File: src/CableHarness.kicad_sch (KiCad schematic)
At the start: 14 parts, among them J93 Car Socket

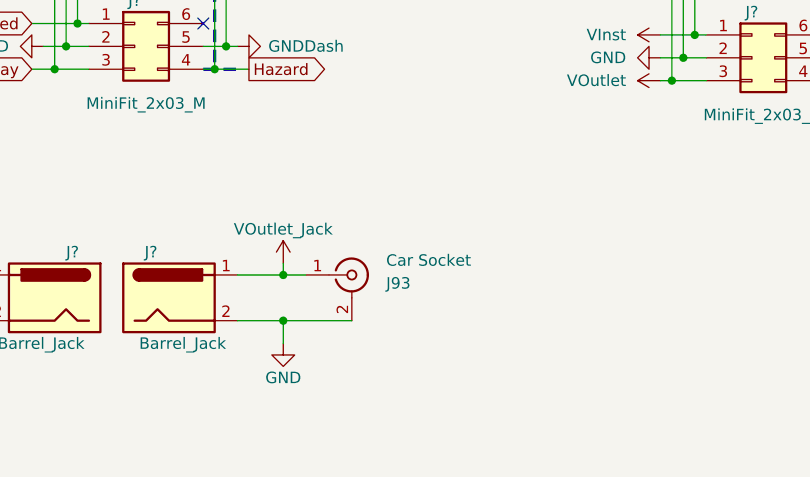
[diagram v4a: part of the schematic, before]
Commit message: Update Schematics; Replace xor with quad nand; Update PCB
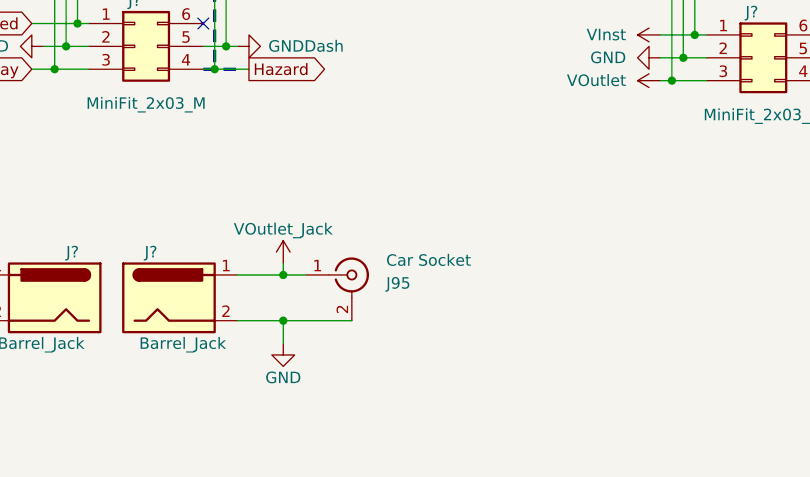
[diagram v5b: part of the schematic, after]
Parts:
- renumbered J93 to J95
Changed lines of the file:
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@@
   (symbol (lib_id "Connector:Conn_Coaxial") (at 195.58 148.59 0) (unit 1)
     (in_bom yes) (on_board yes) (dnp no) (fields_autoplaced)
-    (property "Reference" "J93" (at 199.39 149.5182 0)
+    (property "Reference" "J95" (at 199.39 149.5182 0)
       (effects (font (size 1.27 1.27)) (justify left))
     )
@@
       (project "dragstar-infotainment"
         (path "/e63e39d7-6ac0-4ffd-8aa3-1841a4541b55/74c2db39-21c2-4028-99b6-acc90560d53b"
-          (reference "J93") (unit 1)
+          (reference "J95") (unit 1)
         )
       )
@@
         )
         (path "/e63e39d7-6ac0-4ffd-8aa3-1841a4541b55/74c2db39-21c2-4028-99b6-acc90560d53b"
-          (reference "J87") (unit 1)
+          (reference "J89") (unit 1)
         )
       )
@@
         )
         (path "/e63e39d7-6ac0-4ffd-8aa3-1841a4541b55/74c2db39-21c2-4028-99b6-acc90560d53b"
-          (reference "J88") (unit 1)
+          (reference "J90") (unit 1)
         )
       )
@@
         )
         (path "/e63e39d7-6ac0-4ffd-8aa3-1841a4541b55/74c2db39-21c2-4028-99b6-acc90560d53b"
-          (reference "J86") (unit 1)
+          (reference "J88") (unit 1)
         )
       )
@@
         )
         (path "/e63e39d7-6ac0-4ffd-8aa3-1841a4541b55/74c2db39-21c2-4028-99b6-acc90560d53b"
-          (reference "J92") (unit 1)
+          (reference "J94") (unit 1)
         )
         (path "/e63e39d7-6ac0-4ffd-8aa3-1841a4541b55/5d40715c-dfc9-4b95-9cc7-adbd4b609d9b"
@@
         )
         (path "/e63e39d7-6ac0-4ffd-8aa3-1841a4541b55/74c2db39-21c2-4028-99b6-acc90560d53b"
-          (reference "J85") (unit 1)
+          (reference "J87") (unit 1)
         )
       )
@@
         )
         (path "/e63e39d7-6ac0-4ffd-8aa3-1841a4541b55/74c2db39-21c2-4028-99b6-acc90560d53b"
-          (reference "J84") (unit 1)
+          (reference "J86") (unit 1)
         )
       )
@@
         )
         (path "/e63e39d7-6ac0-4ffd-8aa3-1841a4541b55/74c2db39-21c2-4028-99b6-acc90560d53b"
-          (reference "J91") (unit 1)
+          (reference "J93") (unit 1)
         )
       )
@@
         )
         (path "/e63e39d7-6ac0-4ffd-8aa3-1841a4541b55/74c2db39-21c2-4028-99b6-acc90560d53b"
-          (reference "J90") (unit 1)
+          (reference "J92") (unit 1)
         )
       )
@@
         )
         (path "/e63e39d7-6ac0-4ffd-8aa3-1841a4541b55/74c2db39-21c2-4028-99b6-acc90560d53b"
-          (reference "J83") (unit 1)
+          (reference "J85") (unit 1)
         )
       )
@@
         )
         (path "/e63e39d7-6ac0-4ffd-8aa3-1841a4541b55/74c2db39-21c2-4028-99b6-acc90560d53b"
-          (reference "J82") (unit 1)
+          (reference "J84") (unit 1)
         )
       )
@@
         )
         (path "/e63e39d7-6ac0-4ffd-8aa3-1841a4541b55/74c2db39-21c2-4028-99b6-acc90560d53b"
-          (reference "J94") (unit 1)
+          (reference "J96") (unit 1)
         )
       )
@@
         )
         (path "/e63e39d7-6ac0-4ffd-8aa3-1841a4541b55/74c2db39-21c2-4028-99b6-acc90560d53b"
-          (reference "J89") (unit 1)
+          (reference "J91") (unit 1)
         )
         (path "/e63e39d7-6ac0-4ffd-8aa3-1841a4541b55/5d40715c-dfc9-4b95-9cc7-adbd4b609d9b"
@@
         )
         (path "/e63e39d7-6ac0-4ffd-8aa3-1841a4541b55/74c2db39-21c2-4028-99b6-acc90560d53b"
-          (reference "J95") (unit 1)
-        )
-      )
+          (reference "J97") (unit 1)
+        )
+      )

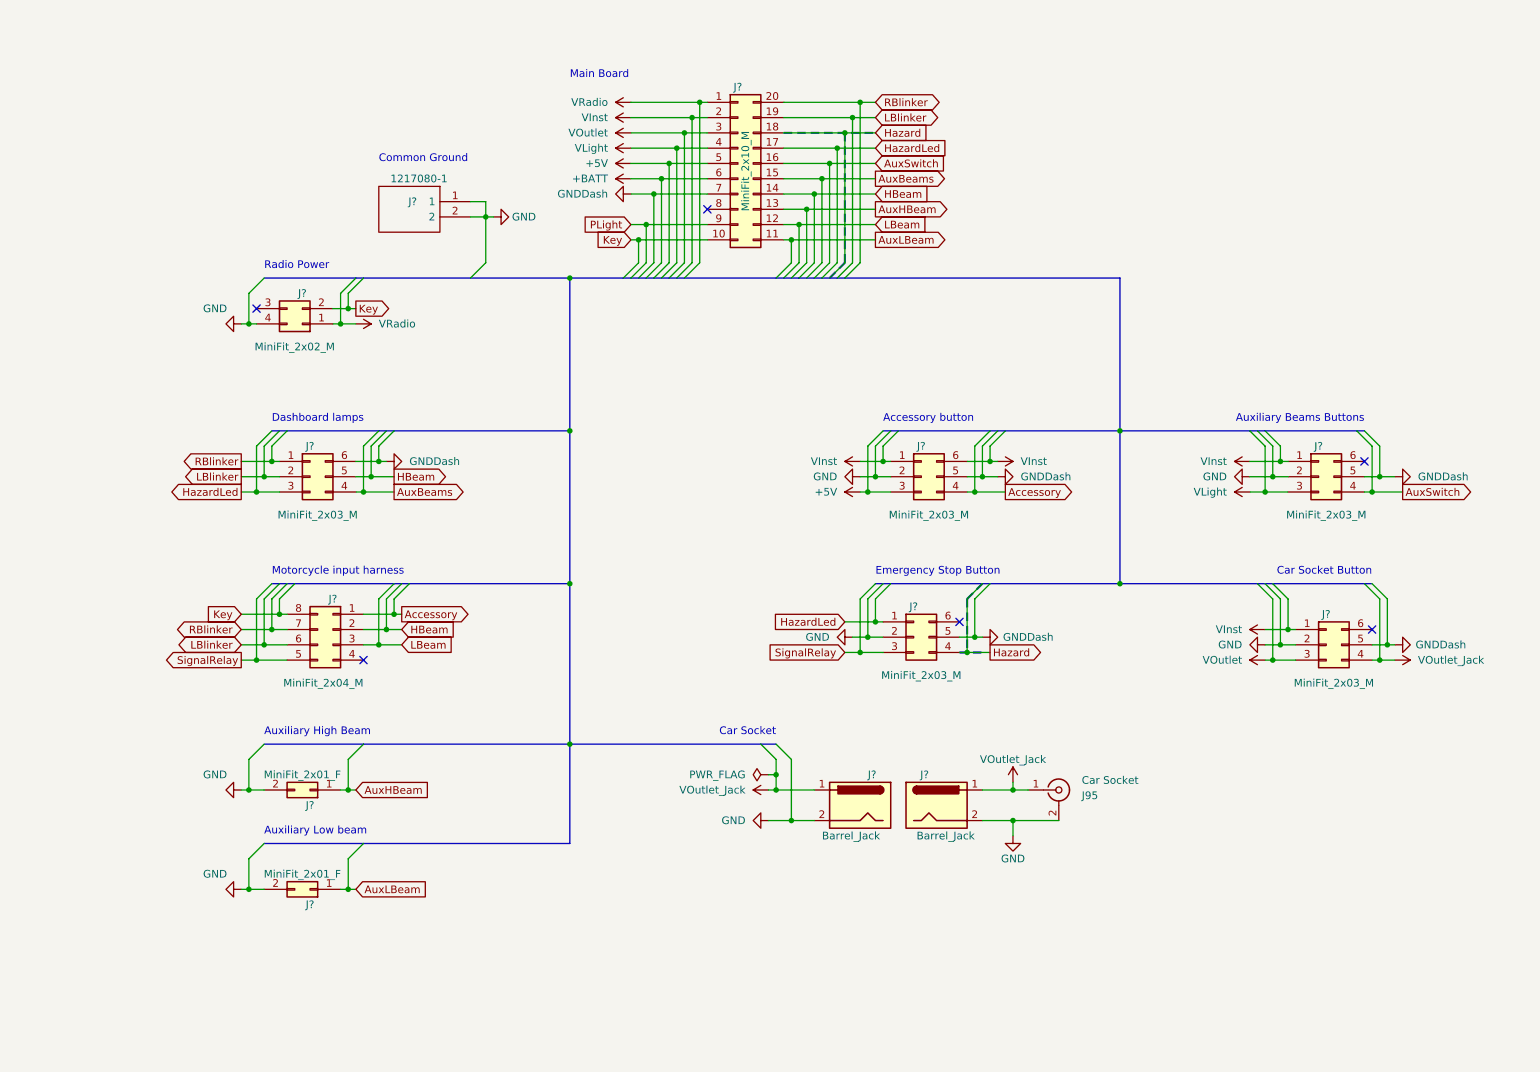
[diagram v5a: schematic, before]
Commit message: simplify circuit diagram. Remove unecessary features; Split board into two components|
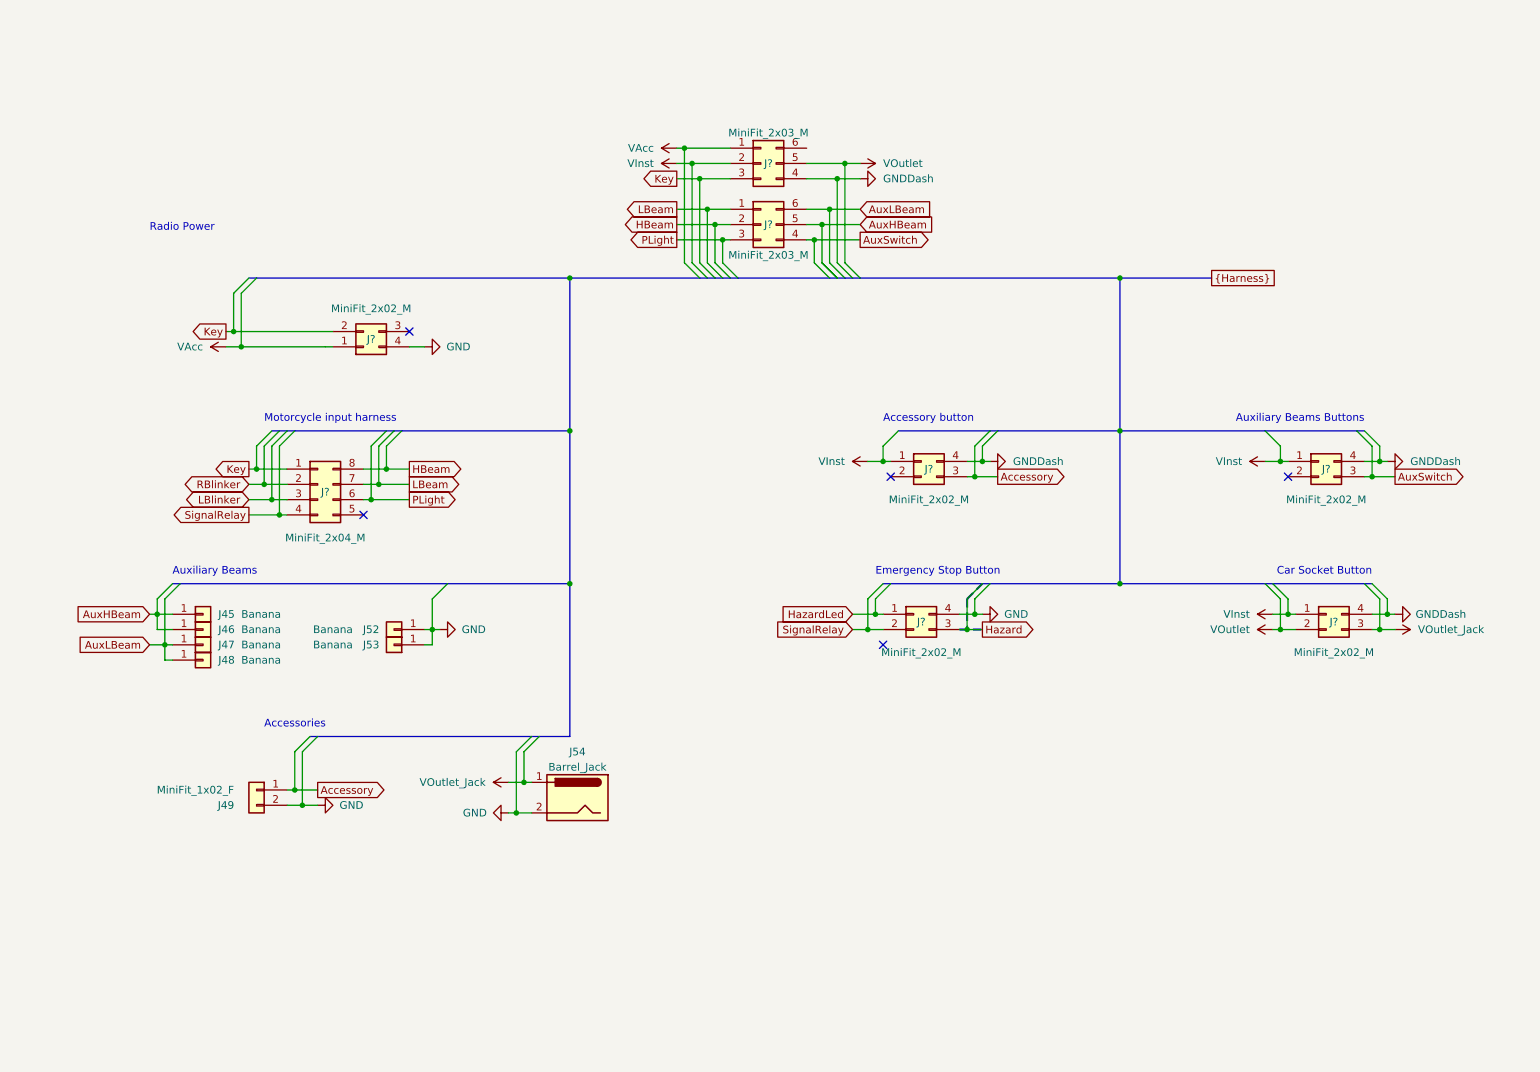
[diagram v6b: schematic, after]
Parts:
- removed J95: Car Socket, symbol Connector:Conn_Coaxial
- removed J?: 1217080-1, 1217080-1, symbol SamacSys_Parts:1217080-1
- removed J?: MiniFit_2x10_M, symbol Connector_Generic:Conn_02x10_Counter_Clockwise
- removed J?: MiniFit_2x04_M, Connector_Molex:Molex_Mini-Fit_Jr_5566-08A_2x04_P4.20mm_Vertical, symbol Connector_Generic:Conn_02x04_Counter_Clockwise
- removed J? (x2): Barrel_Jack, Connector_BarrelJack:BarrelJack_CUI_PJ-063AH_Horizontal, symbol Connector:Barrel_Jack
- removed J? (x2): MiniFit_2x01_F, Connector_Molex:Molex_Mini-Fit_Jr_5566-02A_2x01_P4.20mm_Vertical, symbol Connector_Generic:Conn_02x01
- removed J? (x5): MiniFit_2x03_M, Connector_Molex:Molex_Mini-Fit_Jr_5566-06A_2x03_P4.20mm_Vertical, symbol Connector_Generic:Conn_02x03_Counter_Clockwise
- removed J?: MiniFit_2x02_M, Connector_Molex:Molex_Mini-Fit_Jr_5566-04A_2x02_P4.20mm_Vertical, symbol Connector_Generic:Conn_02x02_Counter_Clockwise
- added J45, J46, J47, J48, J52, J53: Banana, symbol Connector_Generic:Conn_01x01
- added J49: MiniFit_1x02_F, symbol Connector_Generic:Conn_01x02
- added J54: Barrel_Jack, symbol Connector:Barrel_Jack
- added J?: MiniFit_2x04_M, symbol Connector_Generic:Conn_02x04_Counter_Clockwise
- added J? (x5): MiniFit_2x02_M, symbol Connector_Generic:Conn_02x02_Counter_Clockwise
- added J? (x2): MiniFit_2x03_M, symbol Connector_Generic:Conn_02x03_Counter_Clockwise
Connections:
- net Accessory: now also J49.1 (Pin_1), J?.3 (Pin_3)
- net AuxHBeam: now also J45.1 (Pin_1), J46.1 (Pin_1), J?.5 (Pin_5)
- net AuxLBeam: now also J47.1 (Pin_1), J48.1 (Pin_1), J?.6 (Pin_6)
- net AuxSwitch: now also J?.3 (Pin_3), J?.4 (Pin_4)
- net GND: now also J49.2 (Pin_2), J52.1 (Pin_1), J53.1 (Pin_1), J54.2, J?.4 (Pin_4), J?.4 (Pin_4)
- net GNDDash: now also J?.4 (Pin_4), J?.4 (Pin_4), J?.4 (Pin_4), J?.4 (Pin_4)
- net HBeam: now also J?.2 (Pin_2), J?.8 (Pin_8)
- net Hazard: now also J?.3 (Pin_3)
- net HazardLed: now also J?.1 (Pin_1)
- net Key: now also J?.1 (Pin_1), J?.2 (Pin_2), J?.3 (Pin_3)
- net LBeam: now also J?.1 (Pin_1), J?.7 (Pin_7)
- net LBlinker: now also J?.3 (Pin_3)
- net PLight: now also J?.3 (Pin_3), J?.6 (Pin_6)
- net RBlinker: now also J?.2 (Pin_2)
- net SignalRelay: now also J?.2 (Pin_2), J?.4 (Pin_4)
- net VInst: now also J?.1 (Pin_1), J?.1 (Pin_1), J?.1 (Pin_1), J?.2 (Pin_2)
- net VOutlet: now also J?.2 (Pin_2), J?.5 (Pin_5)
- net VOutlet_Jack: now also J54.1, J?.3 (Pin_3)
- new net VAcc: J?.1 (Pin_1), J?.1 (Pin_1)
- no-connect marks 6 -> 5
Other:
- note added: "Accessories"
- note added: "Auxiliary Beams"
- note removed: "Auxiliary High Beam"
- note removed: "Auxiliary Low beam"
- note removed: "Car Socket"
- note removed: "Common Ground"
- note removed: "Dashboard lamps"
- note removed: "Main Board"

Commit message: Simplify circuit diagram. Remove unecessary features
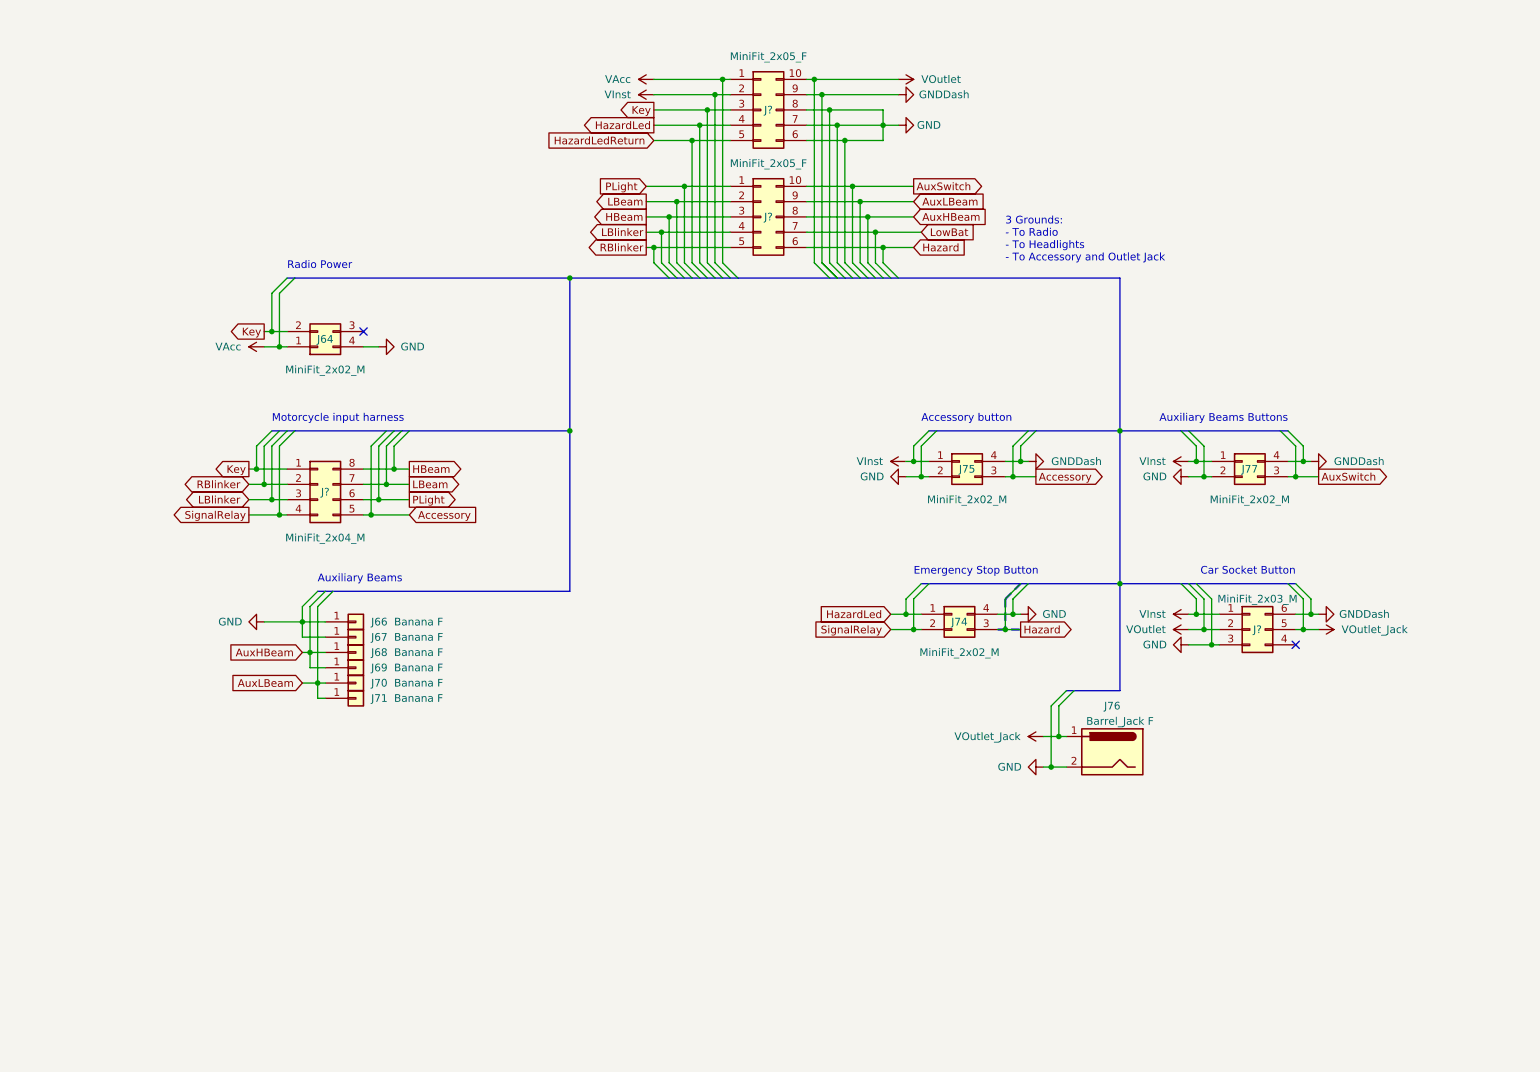
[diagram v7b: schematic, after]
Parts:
- removed J49: MiniFit_1x02_F, symbol Connector_Generic:Conn_01x02
- removed J?: MiniFit_2x02_M, symbol Connector_Generic:Conn_02x02_Counter_Clockwise
- removed J? (x2): MiniFit_2x03_M, symbol Connector_Generic:Conn_02x03_Counter_Clockwise
- added J? (x2): MiniFit_2x05_F, Connector_Molex:Molex_Mini-Fit_Jr_5566-10A_2x05_P4.20mm_Vertical, symbol Connector_Generic:Conn_02x05_Counter_Clockwise
- added J?: MiniFit_2x03_M, symbol Connector_Generic:Conn_02x03_Counter_Clockwise
- J66: renamed from J52; value Banana -> Banana F
- J67: renamed from J53; value Banana -> Banana F
- J68: renamed from J45; value Banana -> Banana F
- J69: renamed from J46; value Banana -> Banana F
- J70: renamed from J47; value Banana -> Banana F
- J71: renamed from J48; value Banana -> Banana F
- J76: renamed from J54; value Barrel_Jack -> Barrel_Jack F
- gave numbers to parts that had none: 4
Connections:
- net Accessory: now also J?.5 (Pin_5)
- net AuxHBeam: now also J?.8 (Pin_8)
- net AuxLBeam: now also J?.9 (Pin_9)
- net AuxSwitch: now also J?.10 (Pin_10)
- net GND: now also J75.2 (Pin_2), J77.2 (Pin_2), J?.3 (Pin_3), J?.6 (Pin_6), J?.7 (Pin_7), J?.8 (Pin_8)
- net GNDDash: now also J?.6 (Pin_6), J?.9 (Pin_9)
- net HBeam: now also J?.3 (Pin_3)
- net Hazard: now also J?.6 (Pin_6)
- net HazardLed: now also J?.4 (Pin_4)
- net Key: now also J?.3 (Pin_3)
- net LBeam: now also J?.2 (Pin_2)
- net LBlinker: now also J?.4 (Pin_4)
- net PLight: now also J?.1 (Pin_1)
- net RBlinker: now also J?.5 (Pin_5)
- net VAcc: now also J?.1 (Pin_1)
- net VInst: now also J?.1 (Pin_1), J?.2 (Pin_2)
- net VOutlet: now also J?.10 (Pin_10), J?.2 (Pin_2)
- net VOutlet_Jack: now also J?.5 (Pin_5)
- new net HazardLedReturn: J?.5 (Pin_5)
- new net LowBat: J?.7 (Pin_7)
- no-connect marks 5 -> 2
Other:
- note added: "3 Grounds: - To Radio - To Headlights - To Accessory and Outlet Jack"
- note removed: "Accessories"
- moved on the sheet: J64, J66, J67, J68, J69, J70, J71, J74, J75, J76, J77
